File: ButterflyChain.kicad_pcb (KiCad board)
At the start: 2 copper layers, 93.1 x 65.5 mm, 25 parts, among them J1 Input, J2 Output, J3 Antennae

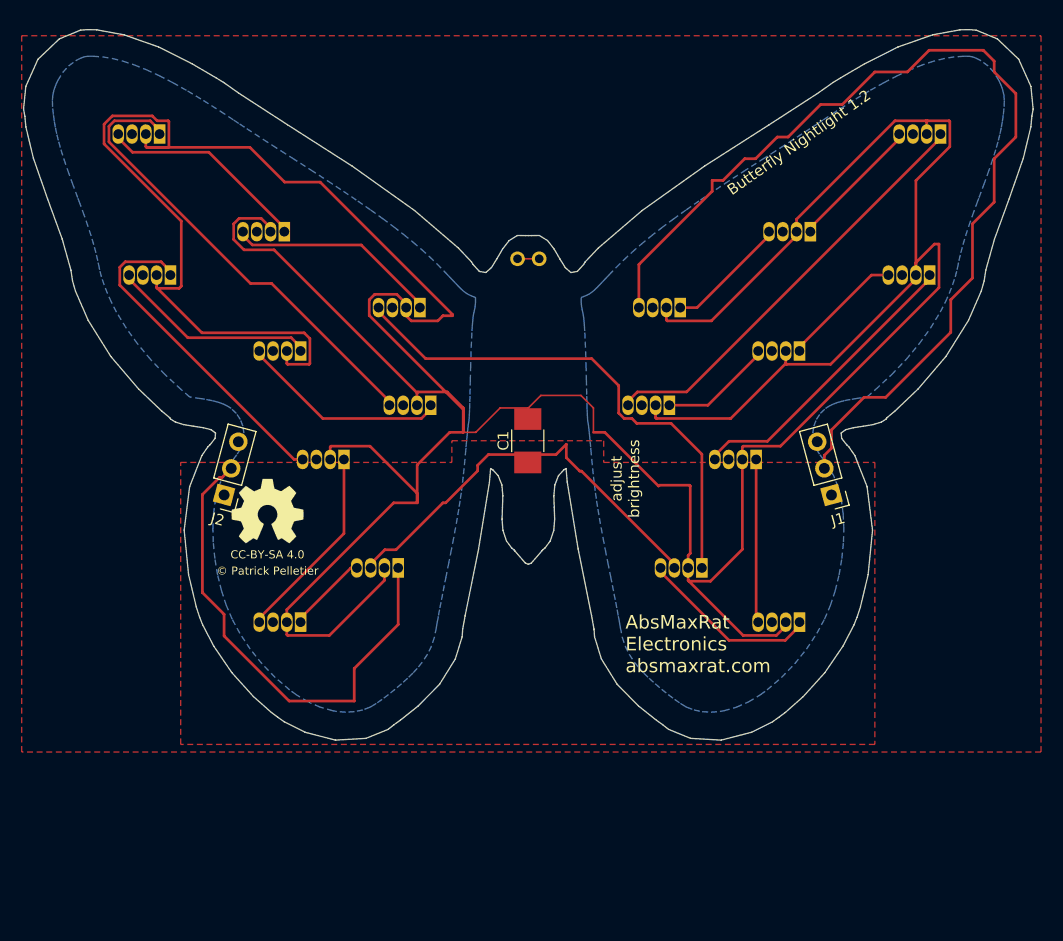
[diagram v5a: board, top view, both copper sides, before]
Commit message: Change how data tracks are routed.
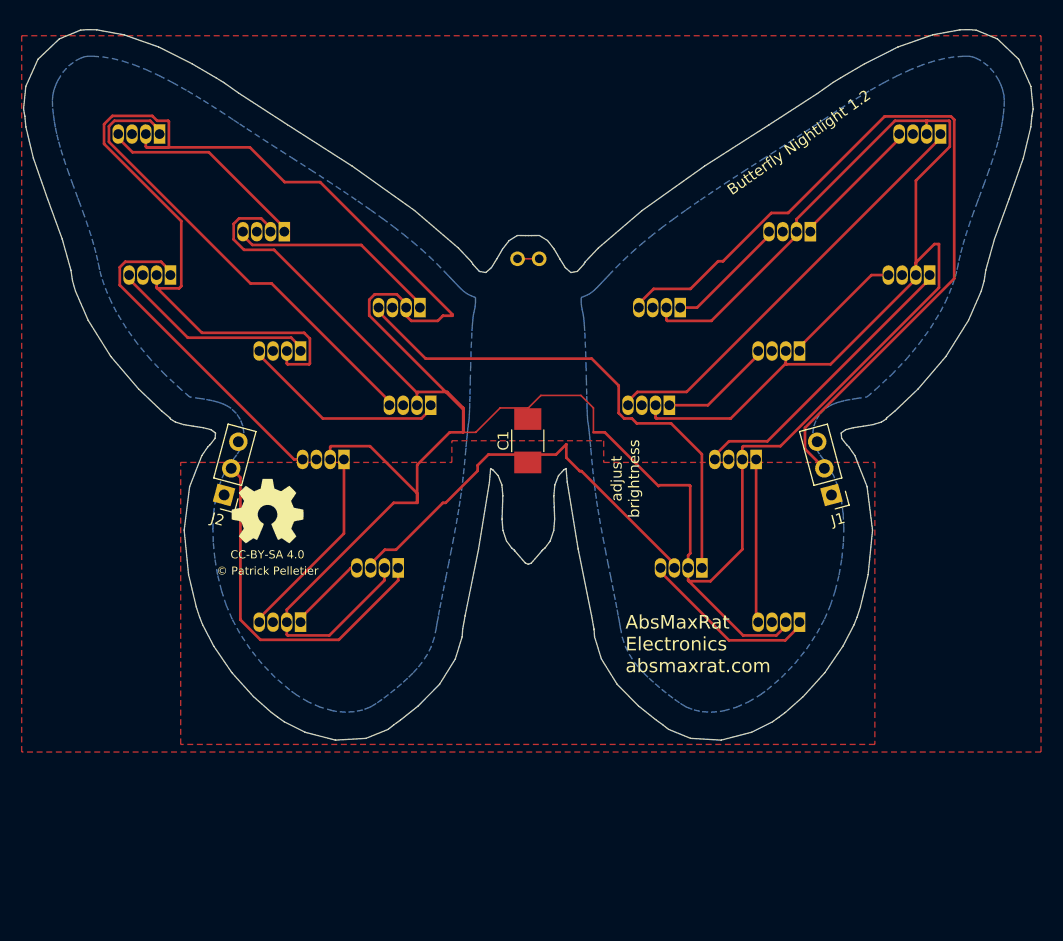
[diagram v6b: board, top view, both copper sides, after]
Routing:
- net Net-(D1-Pad4): track 93.1 -> 75.3 mm
- net Net-(D18-Pad1): track 46.0 -> 33.0 mm
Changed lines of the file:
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@@
     (thickness 1.6)
     (drawings 187)
-    (tracks 272)
+    (tracks 250)
     (zones 0)
     (modules 25)
@@
   (segment (start 115.608006 98.72564) (end 122.243006 92.09064) (width 0.25) (layer F.Cu) (net 3) (status 20))
   (segment (start 122.243006 92.09064) (end 122.243006 91.72564) (width 0.25) (layer F.Cu) (net 3) (status 30))
-  (segment (start 117 88) (end 110.243006 94.756994) (width 0.254) (layer F.Cu) (net 4))
-  (segment (start 110.243006 94.756994) (end 110.243006 98.72564) (width 0.254) (layer F.Cu) (net 4) (status 20))
-  (segment (start 117 87) (end 117 88) (width 0.254) (layer F.Cu) (net 4))
-  (segment (start 118 87) (end 117 87) (width 0.254) (layer F.Cu) (net 4))
-  (segment (start 120 85) (end 118 87) (width 0.254) (layer F.Cu) (net 4))
-  (segment (start 121 85) (end 120 85) (width 0.254) (layer F.Cu) (net 4))
-  (segment (start 123 83) (end 121 85) (width 0.254) (layer F.Cu) (net 4))
-  (segment (start 124 83) (end 123 83) (width 0.254) (layer F.Cu) (net 4))
-  (segment (start 127 80) (end 124 83) (width 0.254) (layer F.Cu) (net 4))
-  (segment (start 129 80) (end 127 80) (width 0.254) (layer F.Cu) (net 4))
-  (segment (start 132 77) (end 129 80) (width 0.254) (layer F.Cu) (net 4))
-  (segment (start 135 77) (end 132 77) (width 0.254) (layer F.Cu) (net 4))
-  (segment (start 137 75) (end 135 77) (width 0.254) (layer F.Cu) (net 4))
-  (segment (start 142 75) (end 137 75) (width 0.254) (layer F.Cu) (net 4))
-  (segment (start 143 76) (end 142 75) (width 0.254) (layer F.Cu) (net 4))
-  (segment (start 143 77) (end 143 76) (width 0.254) (layer F.Cu) (net 4))
-  (segment (start 145 79) (end 143 77) (width 0.254) (layer F.Cu) (net 4))
-  (segment (start 145 83) (end 145 79) (width 0.254) (layer F.Cu) (net 4))
-  (segment (start 143 85) (end 145 83) (width 0.254) (layer F.Cu) (net 4))
-  (segment (start 143 89) (end 143 85) (width 0.254) (layer F.Cu) (net 4))
-  (segment (start 141 91) (end 143 89) (width 0.254) (layer F.Cu) (net 4))
-  (segment (start 141 96) (end 141 91) (width 0.254) (layer F.Cu) (net 4))
-  (segment (start 139 98) (end 141 96) (width 0.254) (layer F.Cu) (net 4))
-  (segment (start 139 101) (end 139 98) (width 0.254) (layer F.Cu) (net 4))
-  (segment (start 133 107) (end 139 101) (width 0.254) (layer F.Cu) (net 4))
-  (segment (start 131 107) (end 133 107) (width 0.254) (layer F.Cu) (net 4))
-  (segment (start 128 110) (end 131 107) (width 0.254) (layer F.Cu) (net 4))
-  (segment (start 128 111.687067) (end 128 110) (width 0.254) (layer F.Cu) (net 4))
-  (segment (start 127.3426 113.546548) (end 127.3426 112.344467) (width 0.254) (layer F.Cu) (net 4) (status 10))
-  (segment (start 127.3426 112.344467) (end 128 111.687067) (width 0.254) (layer F.Cu) (net 4))
+  (segment (start 115 97) (end 111.603646 97) (width 0.254) (layer F.Cu) (net 4))
+  (segment (start 111.603646 97) (end 110.243006 98.36064) (width 0.254) (layer F.Cu) (net 4))
+  (segment (start 117.548103 94.451897) (end 115 97) (width 0.254) (layer F.Cu) (net 4))
+  (segment (start 118 94.451897) (end 117.548103 94.451897) (width 0.254) (layer F.Cu) (net 4))
+  (segment (start 124 90) (end 122.451897 90) (width 0.254) (layer F.Cu) (net 4))
+  (segment (start 122.451897 90) (end 118 94.451897) (width 0.254) (layer F.Cu) (net 4))
+  (segment (start 132.903771 81.096229) (end 124 90) (width 0.254) (layer F.Cu) (net 4))
+  (segment (start 127.3426 113.546548) (end 125.555798 111.759746) (width 0.254) (layer F.Cu) (net 4))
+  (segment (start 125.555798 111.759746) (end 125.555798 109.814772) (width 0.254) (layer F.Cu) (net 4))
+  (segment (start 125.555798 109.814772) (end 139.317416 96.053154) (width 0.254) (layer F.Cu) (net 4))
+  (segment (start 139.317416 96.053154) (end 139.317416 81.398126) (width 0.254) (layer F.Cu) (net 4))
+  (segment (start 139.317416 81.398126) (end 139.015519 81.096229) (width 0.254) (layer F.Cu) (net 4))
+  (segment (start 139.015519 81.096229) (end 132.903771 81.096229) (width 0.254) (layer F.Cu) (net 4))
   (segment (start 110.243006 98.36064) (end 110.243006 98.72564) (width 0.25) (layer F.Cu) (net 4) (status 30))
   (segment (start 126.053006 91.72564) (end 126.053006 91.36064) (width 0.25) (layer F.Cu) (net 5) (status 30))
@@
   (segment (start 83.688006 122.72564) (end 84.243006 122.72564) (width 0.25) (layer F.Cu) (net 20) (status 20))
   (segment (start 79.053006 127.36064) (end 83.688006 122.72564) (width 0.25) (layer F.Cu) (net 20) (status 10))
-  (segment (start 72.6574 113.546548) (end 71.807401 114.396547) (width 0.254) (layer F.Cu) (net 21) (status 10))
-  (segment (start 70 125) (end 72 127) (width 0.254) (layer F.Cu) (net 21))
-  (segment (start 88.053006 127.946994) (end 88.053006 122.72564) (width 0.254) (layer F.Cu) (net 21) (status 20))
-  (segment (start 71.807401 114.396547) (end 71.566231 114.396547) (width 0.254) (layer F.Cu) (net 21))
-  (segment (start 71.566231 114.396547) (end 70 115.962778) (width 0.254) (layer F.Cu) (net 21))
-  (segment (start 72 129) (end 78 135) (width 0.254) (layer F.Cu) (net 21))
-  (segment (start 70 115.962778) (end 70 125) (width 0.254) (layer F.Cu) (net 21))
-  (segment (start 84 132) (end 88.053006 127.946994) (width 0.254) (layer F.Cu) (net 21))
-  (segment (start 72 127) (end 72 129) (width 0.254) (layer F.Cu) (net 21))
-  (segment (start 78 135) (end 84 135) (width 0.254) (layer F.Cu) (net 21))
-  (segment (start 84 135) (end 84 132) (width 0.254) (layer F.Cu) (net 21))
+  (segment (start 72.6574 113.546548) (end 73.507399 114.396547) (width 0.254) (layer F.Cu) (net 21))
+  (segment (start 73.507399 114.396547) (end 73.507399 127.506782) (width 0.254) (layer F.Cu) (net 21))
+  (segment (start 73.507399 127.506782) (end 75.355667 129.35505) (width 0.254) (layer F.Cu) (net 21))
+  (segment (start 75.355667 129.35505) (end 82.577596 129.35505) (width 0.254) (layer F.Cu) (net 21))
+  (segment (start 82.577596 129.35505) (end 88.053006 123.87964) (width 0.254) (layer F.Cu) (net 21))
+  (segment (start 88.053006 123.87964) (end 88.053006 122.72564) (width 0.254) (layer F.Cu) (net 21))
   (segment (start 101.053006 94.22564) (end 99.053006 94.22564) (width 0.1524) (layer F.Cu) (net 22) (status 30))
   (zone (net 1) (net_name +5V) (layer B.Cu) (hatch edge 0.508)

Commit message: Change silkscreen.
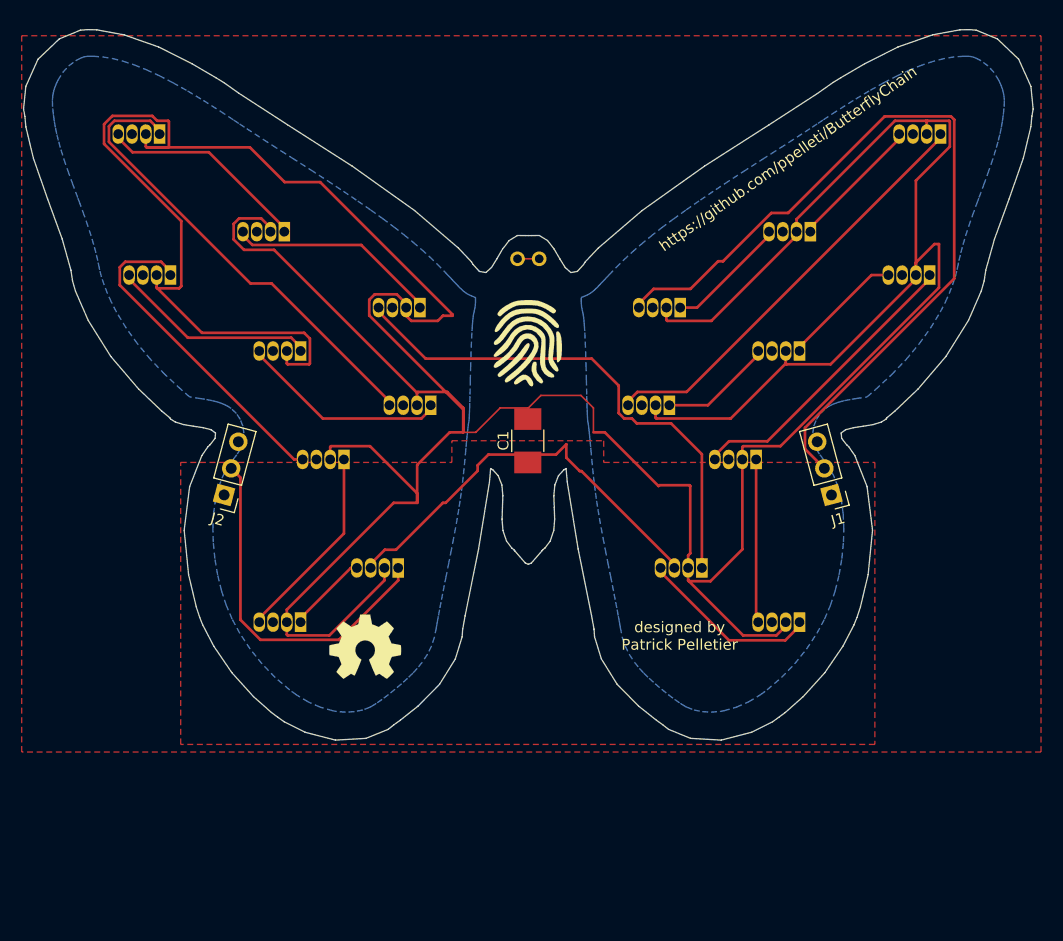
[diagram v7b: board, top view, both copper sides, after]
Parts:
- added G***: LOGO, myLibrary:Fingerprint, F.Cu at (100.0, 102.0)
- moved REF*** 15.4 mm to (85.0, 130.0)
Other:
- board text added: "designed by Patrick Pelletier"
- board text added: "https://github.com/ppelleti/ButterflyChain"
- board text removed: "AbsMaxRat Electronics absmaxrat.com"
- board text removed: "Butterfly Nightlight 1.2"
- board text removed: "CC-BY-SA 4.0"
- board text removed: "adjust brightness"
- board text removed: "© Patrick Pelletier"

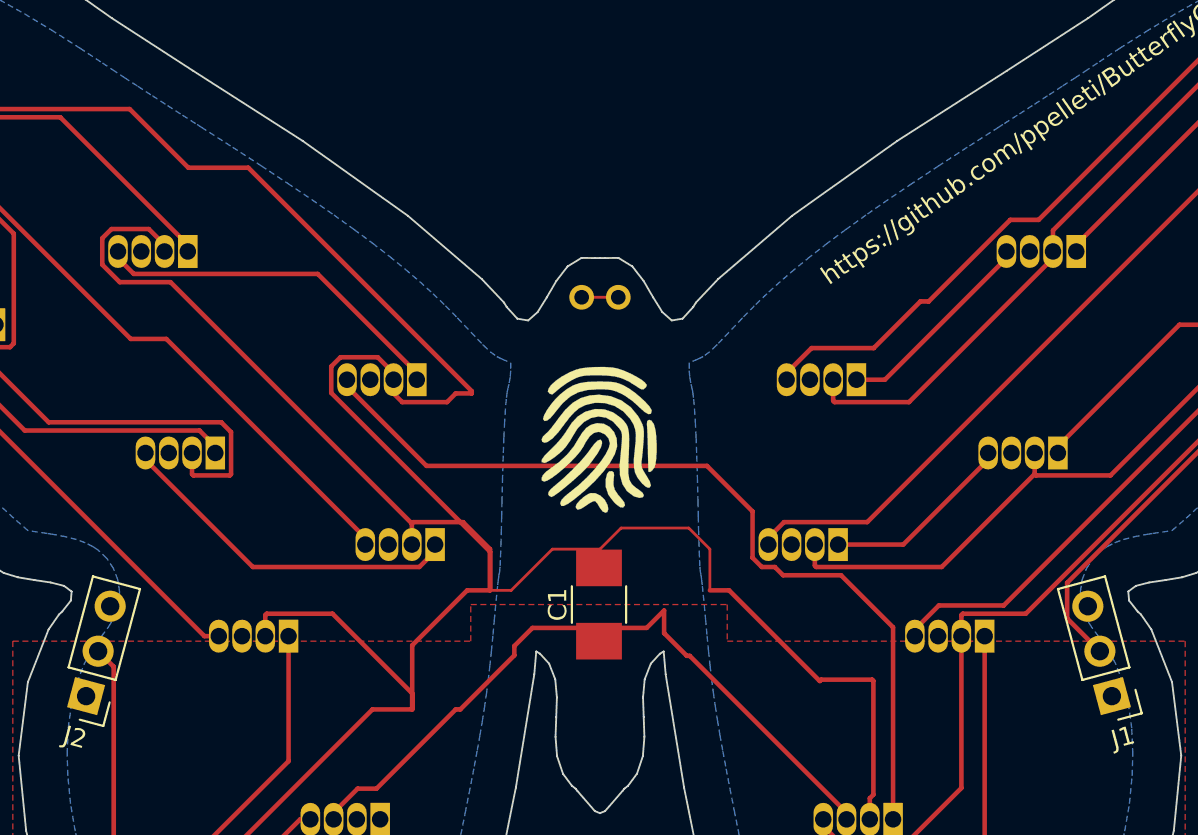
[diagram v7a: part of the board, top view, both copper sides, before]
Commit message: Label input/output pins on silkscreen.
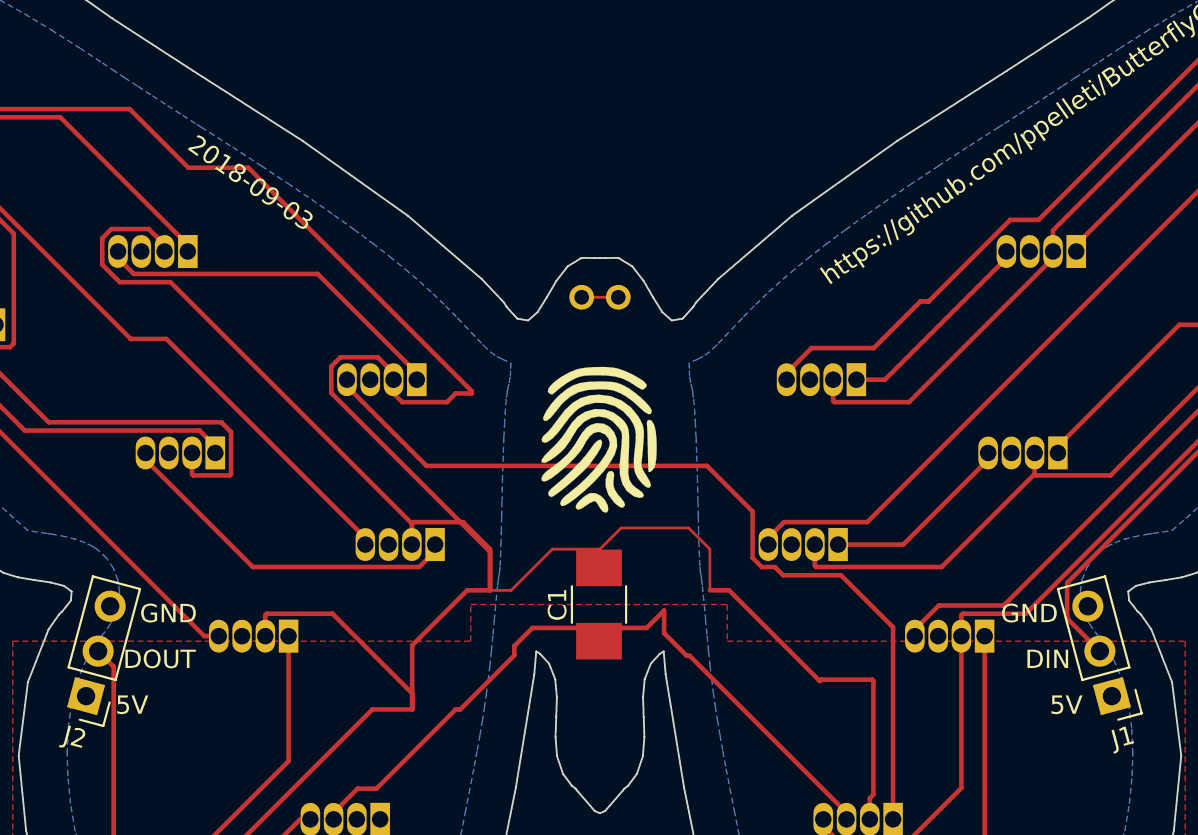
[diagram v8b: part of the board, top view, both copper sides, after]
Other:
- board text added: "2018-09-03"
- board text added: "5V"
- board text added: "DIN"
- board text added: "DOUT"
- board text added: "GND"
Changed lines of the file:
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@@
 (kicad_pcb (version 4) (host pcbnew 4.0.7)
   (general
-    (links 0)
+    (links 60)
     (no_connects 0)
     (area 53.34 73.047739 147.320001 139.700001)
     (thickness 1.6)
-    (drawings 184)
+    (drawings 191)
     (tracks 250)
     (zones 0)
@@
       (xy 0.286924 -3.969467) (xy 0.724974 -3.940798)) (layer F.SilkS) (width 0.01))
   )
+  (gr_text GND (at 123.5 111.5) (layer F.SilkS)
+    (effects (font (size 1 1) (thickness 0.2)))
+  )
+  (gr_text DIN (at 124.5 114) (layer F.SilkS)
+    (effects (font (size 1 1) (thickness 0.2)))
+  )
+  (gr_text 5V (at 125.5 116.5) (layer F.SilkS)
+    (effects (font (size 1 1) (thickness 0.2)))
+  )
+  (gr_text 5V (at 74.5 116.5) (layer F.SilkS)
+    (effects (font (size 1 1) (thickness 0.2)))
+  )
+  (gr_text DOUT (at 76 114) (layer F.SilkS)
+    (effects (font (size 1 1) (thickness 0.2)))
+  )
+  (gr_text GND (at 76.5 111.5) (layer F.SilkS)
+    (effects (font (size 1 1) (thickness 0.2)))
+  )
+  (gr_text 2018-09-03 (at 81 88 325) (layer F.SilkS)
+    (effects (font (size 1 1) (thickness 0.2)))
+  )
   (gr_text "designed by\nPatrick Pelletier" (at 114 129) (layer F.SilkS)
